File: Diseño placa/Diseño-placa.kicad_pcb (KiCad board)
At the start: 2 copper layers, 79 parts, among them IC1 ATMEGA32-P, M1 DIL24, M2 DIL24, M3 DIL16, P1 CONN_01X03, P2 CONN_02X08, P3 CONN_01X01, SW1 SW_PUSH, SW2 SW_PUSH, SW3 SW_PUSH, SW4 SW_PUSH, SW5 SW_PUSH, U1 REG104, U2 OPA625, U3 OPA625, U4 OPA625, U5 OPA625, U6 OPA625, U7 OPA625, X1 16M

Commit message: PCB
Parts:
- added C28: 10n, Capacitors_ThroughHole:C_Rect_L7_W6_P5, F.Cu at (67.0, 103.8)
- added P4: CONN_01X16, Pin_Headers:Pin_Header_Straight_1x16, F.Cu at (143.5, 105.4)
- added P5: CONN_01X05, Pin_Headers:Pin_Header_Straight_1x05, F.Cu at (92.1, 148.6)
- added P6: CONN_01X05, Pin_Headers:Pin_Header_Straight_1x05, F.Cu at (143.5, 52.1)
- added R31: 3.3k, Resistors_ThroughHole:Resistor_Horizontal_RM10mm, F.Cu at (72.7, 98.7)
- P2: footprint Pin_Headers:Pin_Header_Angled_1x16 -> Pin_Headers:Pin_Header_Angled_2x08
- SW1, SW2, SW3, SW4, SW5: footprint Buttons_Switches_ThroughHole:SW_PUSH -> Buttons_Switches_ThroughHole:SW_PUSH-12mm
- U2, U3, U4, U5, U6, U7: footprint Housings_SOT-23_SOT-143_TSOT-6:SC-70-6 -> Housings_SOT-23_SOT-143_TSOT-6:TSOT-6-MK06A_Handsoldering
- X1: footprint Crystals:Crystal_HC48-U_Vertical -> Crystals:Crystal_HC49-U_Vertical
- moved C17 209.0 mm to (63.2, 77.2)
- moved C14 205.9 mm to (47.3, 67.0)
- moved R11 204.6 mm to (41.0, 64.5)
- moved R19 202.9 mm to (58.7, 72.7), turned to 0 degrees
- moved R16 200.5 mm to (53.7, 64.5), turned to 270 degrees
- moved R13 195.9 mm to (44.1, 64.5), turned to 270 degrees
- moved R5 195.1 mm to (37.8, 64.5), turned to 90 degrees
- moved R3 194.0 mm to (34.6, 64.5), turned to 90 degrees
- moved R17 189.8 mm to (50.5, 64.5), turned to 90 degrees
- moved SW3 187.9 mm to (64.8, 169.5)
- moved C10 184.1 mm to (44.8, 56.2), turned to 0 degrees
- moved SW2 183.1 mm to (64.8, 142.9)
- moved U3 181.3 mm to (56.8, 64.5), turned to 180 degrees
- moved C26 177.4 mm to (60.0, 69.5), turned to 180 degrees
- moved R30 174.2 mm to (46.7, 79.1), turned to 90 degrees
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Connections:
- net Net-(DS1-Pad3) renamed /POTE
- C21 pad 1: /ADCIMPEDANCE -> Net-(C21-Pad1)
- M3 pad 1: /x30nA -> /GND
- M3 pad 2: /x120nA -> /GND
- M3 pad 3: /MUX2IO -> /GND
- M3 pad 4: /x200nA -> /GND
- M3 pad 5: /x80nA -> /GND
- P1 pad 1: Net-(P1-Pad1) -> Net-(C5-Pad1)
- P1 pad 2: Net-(C5-Pad1) -> /GND
- P1 pad 3: Net-(P1-Pad3) -> /GND
- R28 pad 1: /ADCIMPEDANCE -> Net-(C21-Pad1)
- U7 pad 1: /ADCIMPEDANCE -> Net-(C21-Pad1)
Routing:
- net /VCC: track 124.2 -> 373.2 mm, vias 0 -> 10
- net /MUX0IO: track 0.00 -> 213.9 mm, vias 0 -> 1
- net /MUX0S0: track 0.00 -> 154.5 mm, vias 0 -> 1
- net /MUX0S1: track 0.00 -> 149.2 mm, vias 0 -> 1
- net /OFFSET: track 193.6 -> 49.1 mm, vias 0 -> 1
- net /MUX1IO: track 22.2 -> 144.0 mm, vias 0 -> 1
- net /GND: track 725.1 -> 614.0 mm, vias 0 -> 8
- net /MUX0S2: track 0.00 -> 107.1 mm, vias 0 -> 1
- net /ADCIMPEDANCE: track 21.5 -> 122.5 mm, vias 0 -> 2
- net /MUX0S3: track 0.00 -> 97.6 mm, vias 0 -> 1
- net Net-(C4-Pad2): track 88.0 -> 3.19 mm
- net /E15: track 0.00 -> 82.6 mm, vias 0 -> 2
- net /E0: track 0.00 -> 82.6 mm, vias 0 -> 2
- net Net-(C5-Pad1): track 94.3 -> 12.5 mm, vias 0 -> 1
- net /BESC: track 0.00 -> 77.7 mm
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- added copper zone on B.Cu, net /GND
- added copper zone on F.Cu, net /GND
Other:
- board outline added: 57.1 x 44.4 mm
- net class Default: via_dia 2 -> 1.7; via_drill 1 -> 0.8

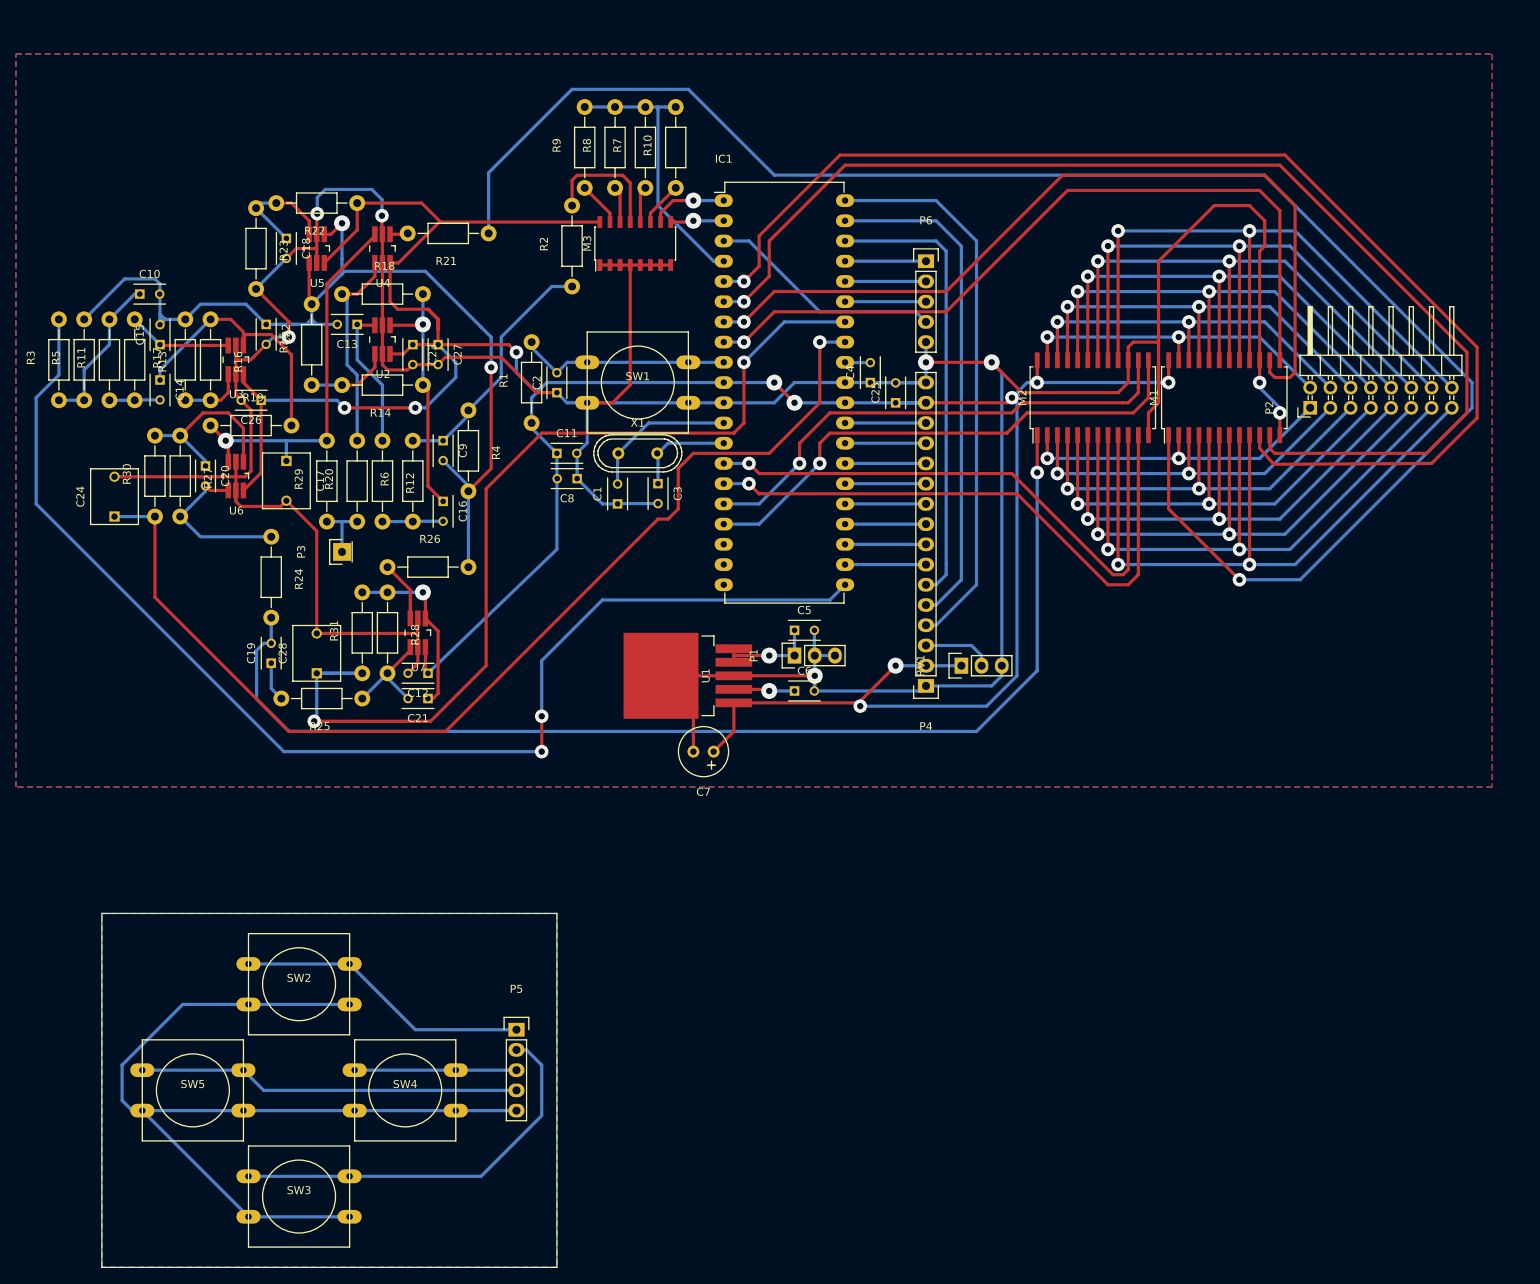
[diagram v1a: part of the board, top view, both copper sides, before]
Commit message: Actualización PCB
*Conector de programación
*Capacitores de los pulsadores
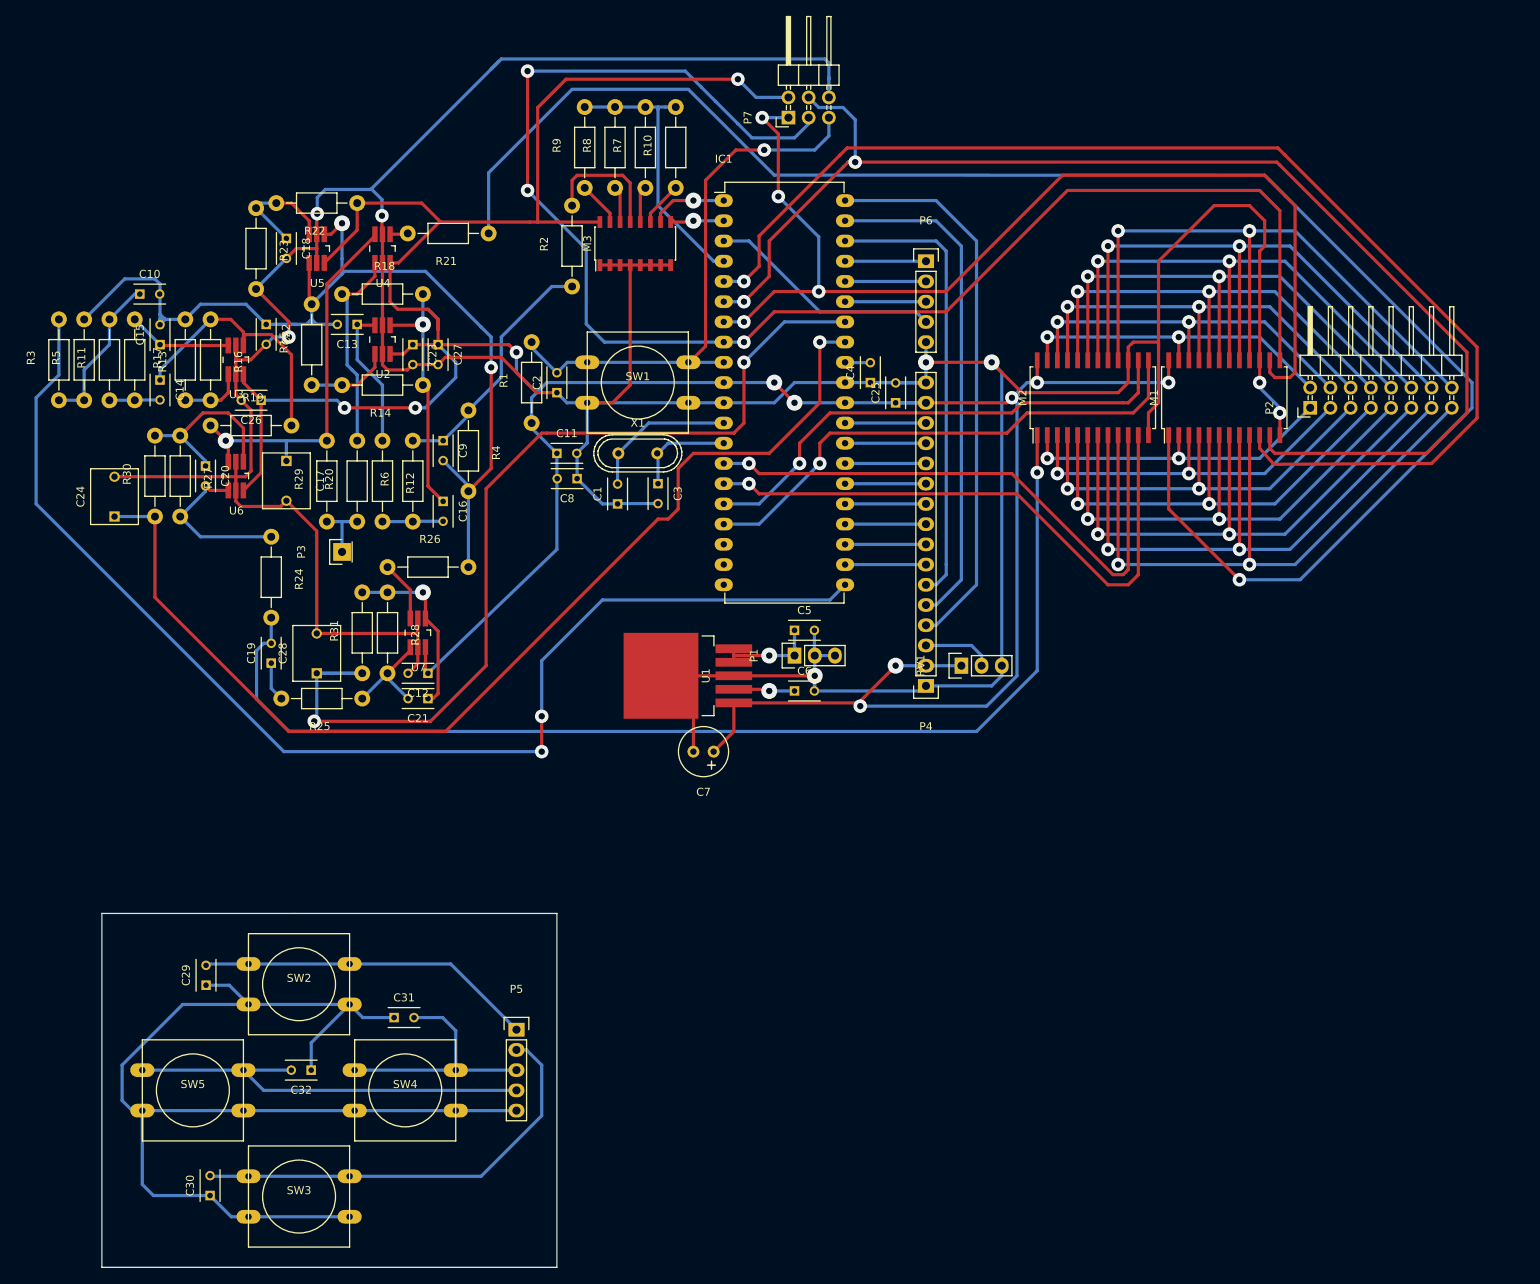
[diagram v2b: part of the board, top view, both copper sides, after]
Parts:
- added C29: 100n, Capacitors_ThroughHole:C_Rect_L4_W2.5_P2.5, F.Cu at (53.1, 143.0)
- added C30: 100n, Capacitors_ThroughHole:C_Rect_L4_W2.5_P2.5, F.Cu at (53.6, 169.4)
- added C31: 100n, Capacitors_ThroughHole:C_Rect_L4_W2.5_P2.5, F.Cu at (76.7, 147.1)
- added C32: 100n, Capacitors_ThroughHole:C_Rect_L4_W2.5_P2.5, F.Cu at (66.3, 153.7)
- added P7: CONN_02X03, Pin_Headers:Pin_Header_Angled_2x03, F.Cu at (126.2, 34.0)
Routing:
- net /GND: track 614.0 -> 712.8 mm
- net /MUX0S3: track 97.6 -> 190.9 mm, vias 1 -> 3
- net /VCC: track 373.2 -> 421.5 mm, vias 10 -> 11
- net /RESET: track 26.7 -> 70.6 mm, vias 0 -> 1
- net /MUX0S2: track 107.1 -> 135.2 mm, vias 1 -> 4
- net /MUX0S1: track 149.2 -> 162.7 mm, vias 1 -> 2
- net /BOK: track 30.5 -> 41.4 mm
- net /BESC: track 77.7 -> 83.7 mm
- net /BUP: track 47.2 -> 52.6 mm
- net /BDOWN: track 60.5 -> 65.3 mm
- net /MUX0S0: track 154.5 -> 155.3 mm
- removed copper zone on B.Cu, net /GND
- removed copper zone on F.Cu, net /GND

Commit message: PCB terminado
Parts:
- P1: footprint Pin_Headers:Pin_Header_Straight_1x03 -> varios:JACK_PWR
- P7: footprint Pin_Headers:Pin_Header_Angled_2x03 -> Pin_Headers:Pin_Header_Straight_2x03
- moved P1 31.0 mm to (97.2, 109.9)
- moved P2 10.6 mm to (200.7, 76.2), turned to 0 degrees
- moved SW1 6.38 mm to (108.0, 61.0), turned to 180 degrees
- moved X1 6.25 mm to (113.0, 73.7), turned to 270 degrees
- moved P7 0.57 mm to (125.7, 34.3)
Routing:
- net /E15: track 82.6 -> 130.4 mm
- net /E14: track 76.7 -> 122.0 mm
- net /GND: track 712.8 -> 757.8 mm, vias 8 -> 5
- net /E13: track 70.8 -> 113.1 mm
- net /E12: track 65.0 -> 103.6 mm
- net /VCC: track 421.5 -> 456.9 mm, vias 11 -> 12
- net /E11: track 59.1 -> 93.4 mm
- net Net-(C5-Pad1): track 12.5 -> 45.0 mm, vias 1 -> 0
- net /E10: track 53.2 -> 85.3 mm
- net /E9: track 47.4 -> 74.7 mm
- net /MUX0S1: track 162.7 -> 137.1 mm
- net /MUX0S0: track 155.3 -> 129.9 mm
- net /E8: track 41.5 -> 64.2 mm
- net /E0: track 82.6 -> 67.7 mm
- net /E1: track 76.7 -> 64.3 mm
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- added copper zone on B.Cu, net /GND
- added copper zone on F.Cu, net /GND
